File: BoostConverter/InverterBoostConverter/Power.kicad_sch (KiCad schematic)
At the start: 84 parts, among them Q1 IPB65R150CFDAATMA1, Q2 IPB65R150CFDAATMA1, Q4 IPB65R150CFDAATMA1, Q5 IPB65R150CFDAATMA1, U1 ACS758xCB-200U-PSF, U3 ACS758xCB-200U-PSF

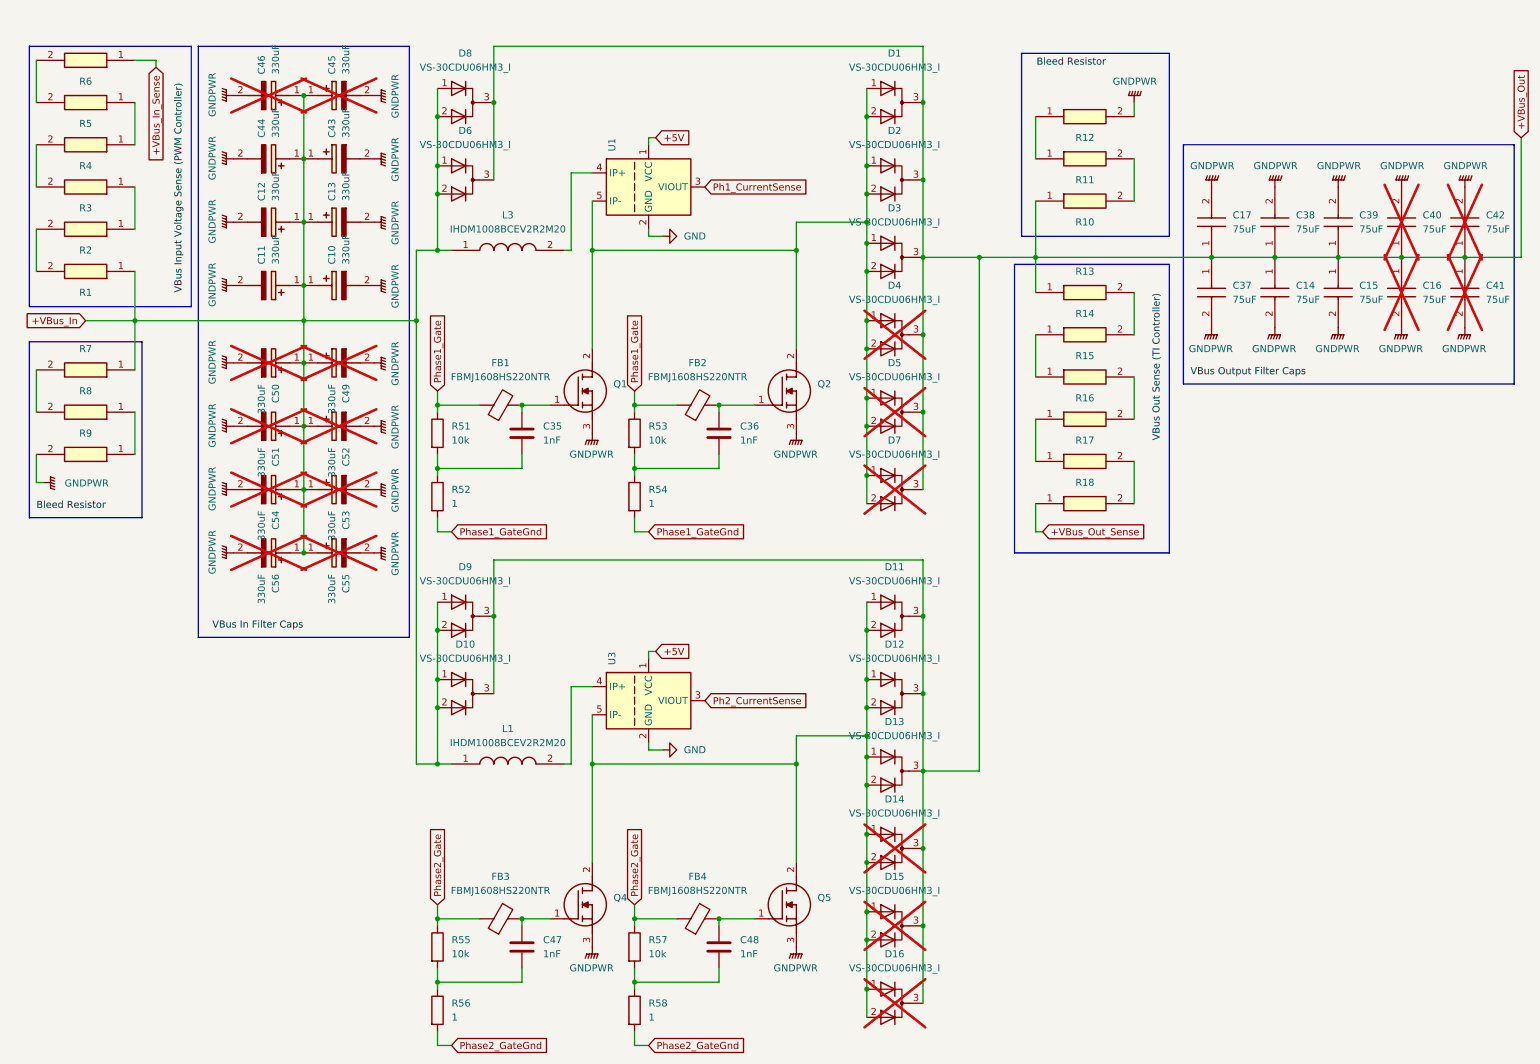
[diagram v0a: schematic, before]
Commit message: Update boost converter, add inverter
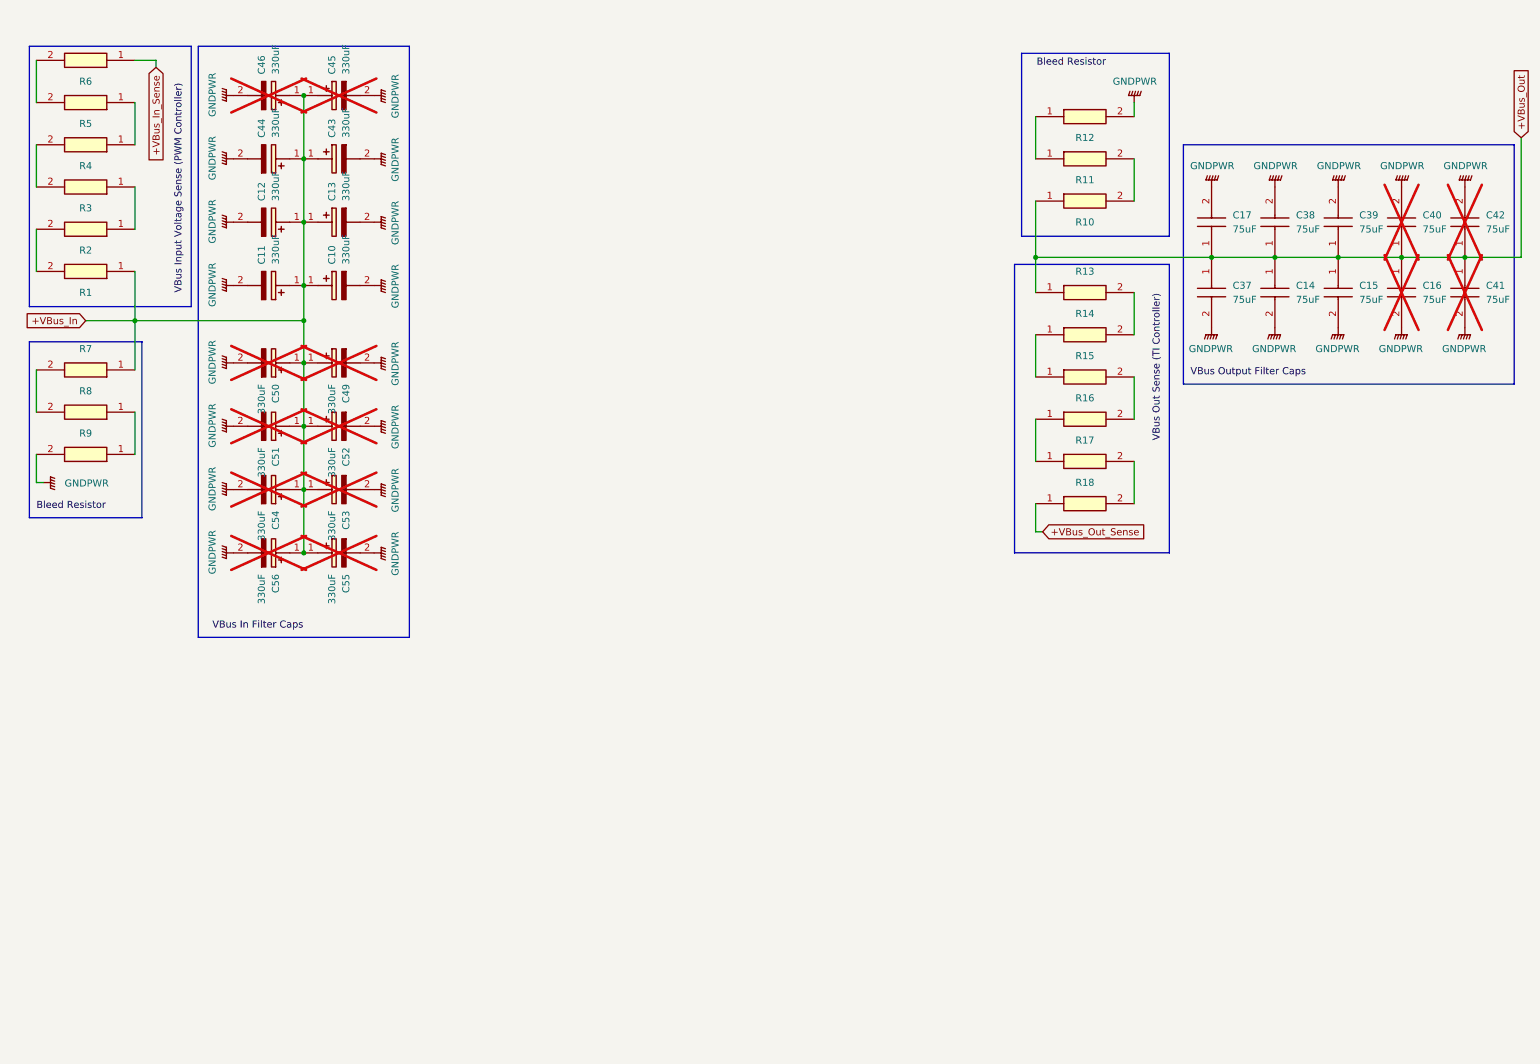
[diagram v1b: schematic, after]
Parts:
- removed C35, C36, C47, C48: 1nF, 1210, symbol Device:C
- removed D1, D10, D11, D12, D13, D14, D15, D16, D2, D3, D4, D5, D6, D7, D8, D9: VS-30CDU06HM3_I, VS30CDU06HM3I, symbol Device:D_Dual_CommonCathode_AAK_Parallel
- removed FB1, FB2, FB3, FB4: FBMJ1608HS220NTR, BEADC1608X100N, symbol Device:FerriteBead
- removed L1, L3: IHDM1008BCEV2R2M20, IHDM1008BCEV2R2M20, symbol InverterCom:IHDM1008BCEV2R2M20
- removed Q1, Q2, Q4, Q5: IPB65R150CFDAATMA1, IPB65R150CFDAATMA1, symbol InverterCom:IPB65R150CFDAATMA1
- removed R51, R53, R55, R57: 10k, 1210, symbol Device:R
- removed R52, R54, R56, R58: 1, 1210, symbol Device:R
- removed U1, U3: ACS758xCB-200U-PSF, Sensor_Current:Allegro_CB_PSF, symbol Sensor_Current:ACS758xCB-200U-PSF

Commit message: Finish Boost Converter
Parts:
- removed C10, C11, C12, C13, C43, C49: 330uF, CAPPRD1000W190D2250H2700, symbol InverterCom:SLPX331M200A1P3
- removed C16, C40, C41, C42: 75uF, ALH82A750CB600, symbol InverterCom:ALH82A750CB600
- C14, C15, C17, C37, C38, C39: footprint ALH82A750CB600 -> InverterCom:ALH82A750CB600
- C44: footprint CAPPRD1000W190D2250H2700 -> InverterCom:CAPPRD1000W190D2250H2700
- C45, C46, C50, C51, C52, C53, C54, C55, C56: footprint CAPPRD1000W190D2250H2700 -> InverterCom:CAPPRD1000W190D2250H2700; now fitted
- R1, R10, R11, R12, R13, R14, R15, R16, R17, R18, R2, R3, R4, R5, R6, R7, R8, R9: footprint RESC6431X65N -> InverterCom:RESC6431X65N
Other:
- moved on the sheet: C44
